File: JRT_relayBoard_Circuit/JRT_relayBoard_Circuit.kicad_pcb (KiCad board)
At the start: 2 copper layers, 100.2 x 63.6 mm, 8 parts, among them J1 Conn_ESP32_Left, J2 Conn_ESP32_Right, J3 eCON_D1-4, J4 eCON_D5-8, J5 eCON_D9-12, J6 eCON_D13-15, J7 eCON_A1-4, J8 eCON_A5_UART_Vin_Vout

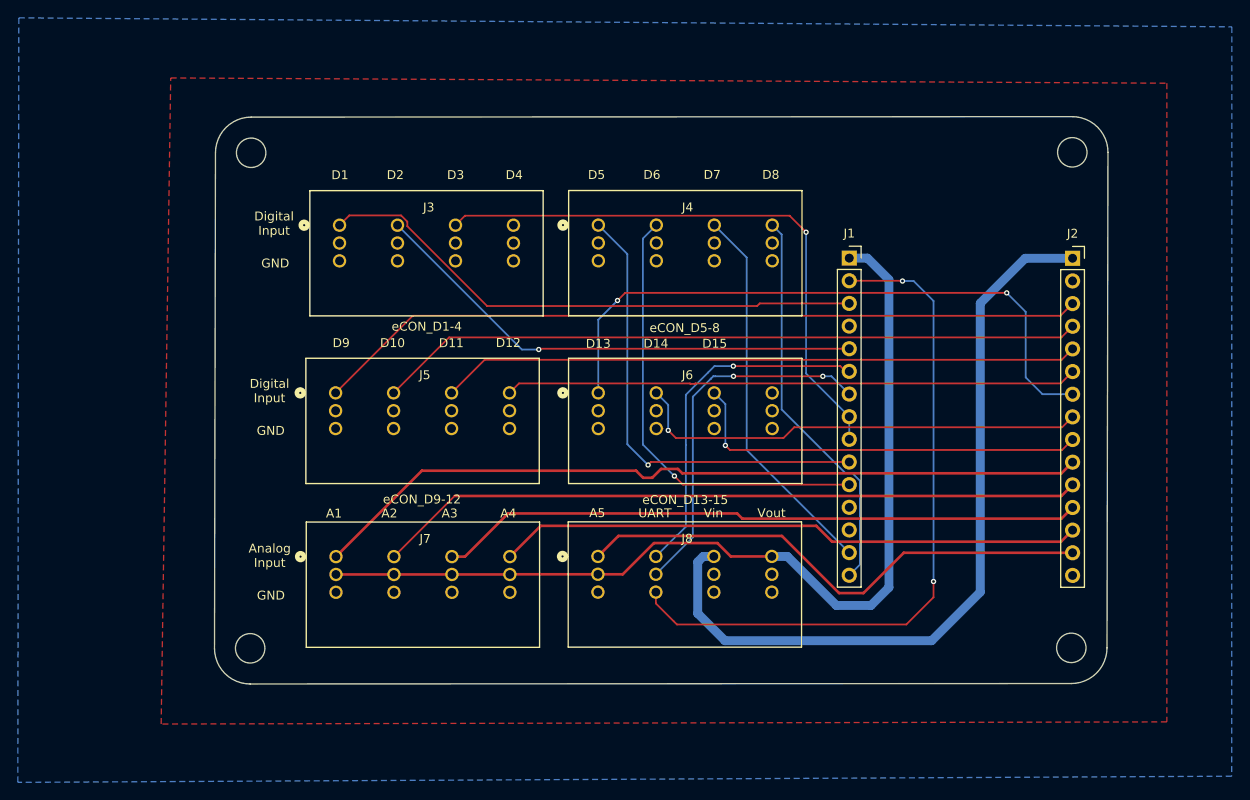
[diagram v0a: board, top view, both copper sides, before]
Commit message: 基板上のシルクを追加
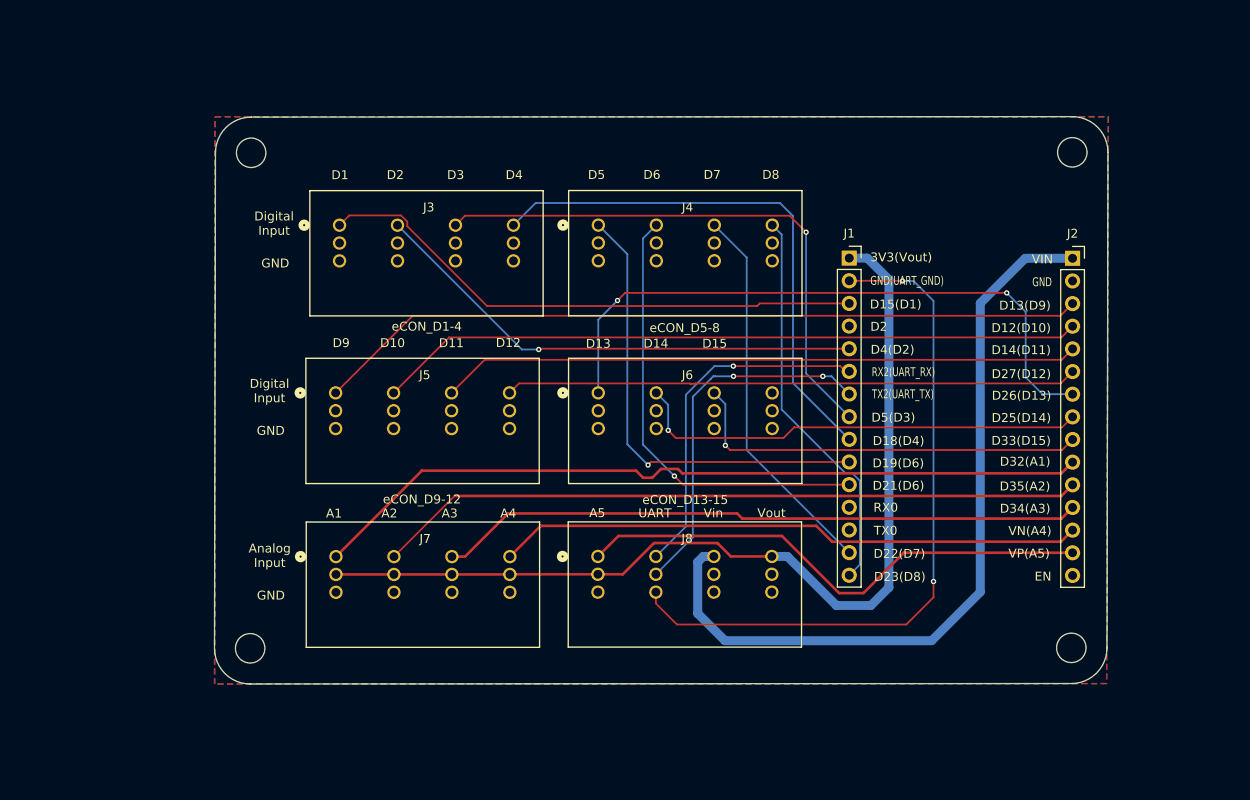
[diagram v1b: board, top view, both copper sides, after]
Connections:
- J1 pad 9: D3 -> D4
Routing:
- net D4: track 0.00 -> 60.6 mm
- net D3: track 65.7 -> 63.2 mm
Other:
- board text added: "3.3V"
- board text added: "3V3(Vout)"
- board text added: "9V"
- board text added: "D12(D10)"
- board text added: "D13(D9)"
- board text added: "D14(D11)"
- board text added: "D15(D1)"
- board text added: "D18(D4)"
- board text added: "D19(D6)"
- board text added: "D21(D6)"
- board text added: "D22(D7)"
- board text added: "D23(D8)"
- board text added: "D25(D14)"
- board text added: "D26(D13)"
- board text added: "D27(D12)"
- board text added: "D32(A1)"
- board text added: "D33(D15)"
- board text added: "D34(A3)"
- board text added: "D35(A2)"
- board text added: "D4(D2)"
- board text added: "D5(D3)"
- board text added: "EN"
- board text added: "GND(UART_GND)"
- board text added: "RX0"
- board text added: "RX2(UART_RX)"
- board text added: "TX0"
- board text added: "TX2(UART_TX)"
- board text added: "UART-GND"
- board text added: "UART-RX"
- board text added: "UART-TX"
- board text added: "VIN"
- board text added: "VN(A4)"
- board text added: "VP(A5)"

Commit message: GNDベタになるように修正
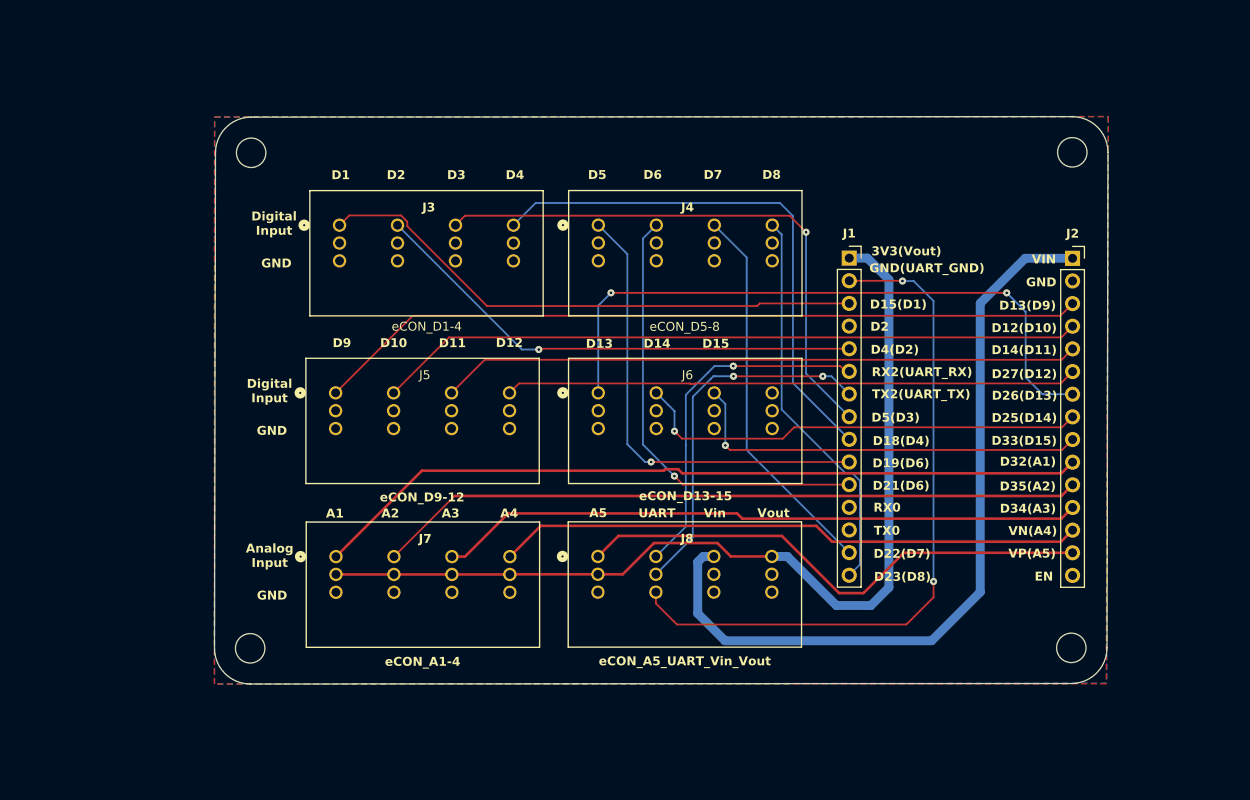
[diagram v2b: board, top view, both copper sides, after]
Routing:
- net D13: track 71.6 -> 72.6 mm
- net A1: track 88.0 -> 87.4 mm
